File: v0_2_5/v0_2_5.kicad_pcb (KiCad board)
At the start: 2 copper layers, 91.4 x 50.8 mm, 58 parts, among them IC1 RASPBERRY_PI_PICO_W, IC2 BH1750FVI-TR, IC3 AP2138N-3.3TRG1, J1 S2B-PH-SM4-TB_LF__SN_, J2 HYCW110-TF10-180B, J4 SM04B-SRSS-TB, J5 Screw_Terminal_01x03, J6 Conn_01x02_Pin, Q1 DMG2301L-7, Q2 DMG2301L-7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

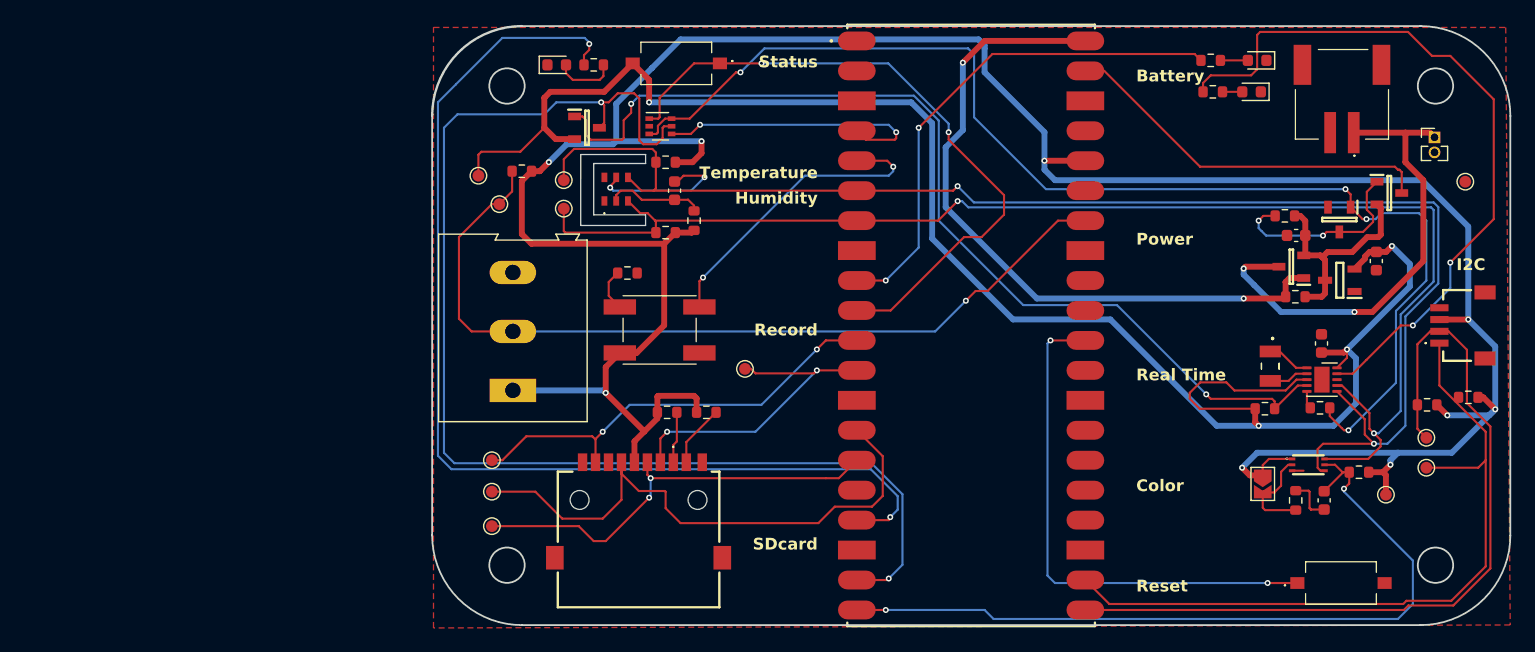
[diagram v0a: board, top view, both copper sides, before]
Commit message: replace sdcard
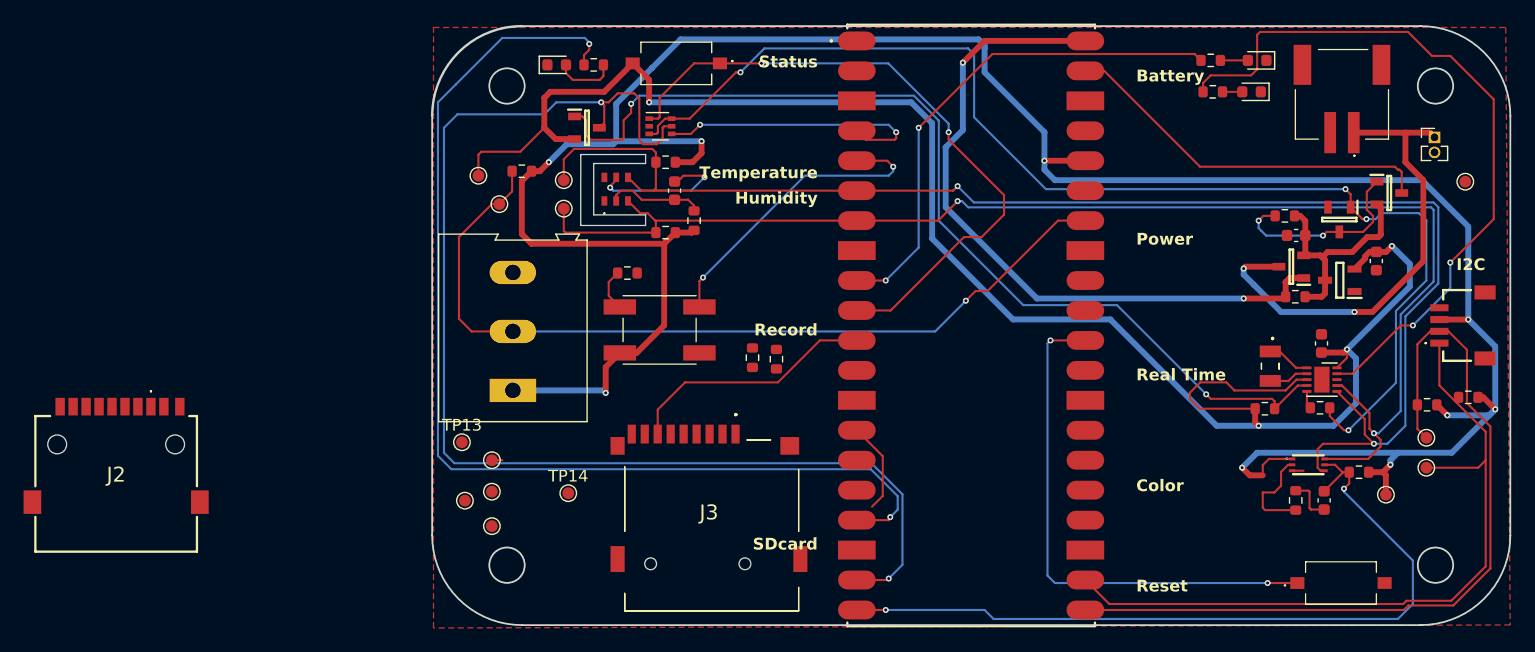
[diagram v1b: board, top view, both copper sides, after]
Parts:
- removed JP1: SolderJumper_2_Open, Jumper:SolderJumper-2_P1.3mm_Open_TrianglePad1.0x1.5mm
- added J3: TF-115, TF-115:TF115, F.Cu at (124.0, 113.1)
- added TP13: TestPoint, TestPoint:TestPoint_Pad_D1.0mm, F.Cu at (103.0, 107.2)
- added TP14: TestPoint, TestPoint:TestPoint_Pad_D1.0mm, F.Cu at (112.0, 111.5)
- moved J2 44.6 mm to (73.7, 110.7)
- moved TP6 26.2 mm to (103.3, 112.1)
- moved R10 8.60 mm to (127.6, 100.0), turned to -90 degrees
- moved R9 7.46 mm to (129.7, 100.1), turned to -90 degrees
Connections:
- J2 pad 1: /SDcard/DAT2 -> /SDcard/CARDDET
- R10 pad 2: /SDcard/DAT2 -> /SDcard/CARDDET
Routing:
- net /SCK: track 48.9 -> 7.76 mm
- net /MOSI: track 36.7 -> 0.00 mm, vias 2 -> 0
- net /CS: track 27.4 -> 0.00 mm, vias 2 -> 0
- net +3.3V: track 231.0 -> 215.4 mm
- net /MISO: track 37.3 -> 22.3 mm, vias 2 -> 0
- net /SDcard/CARDDET: track 5.28 -> 0.00 mm
- net /SDcard/DAT2: track 4.36 -> 0.00 mm

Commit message: replace sdcard
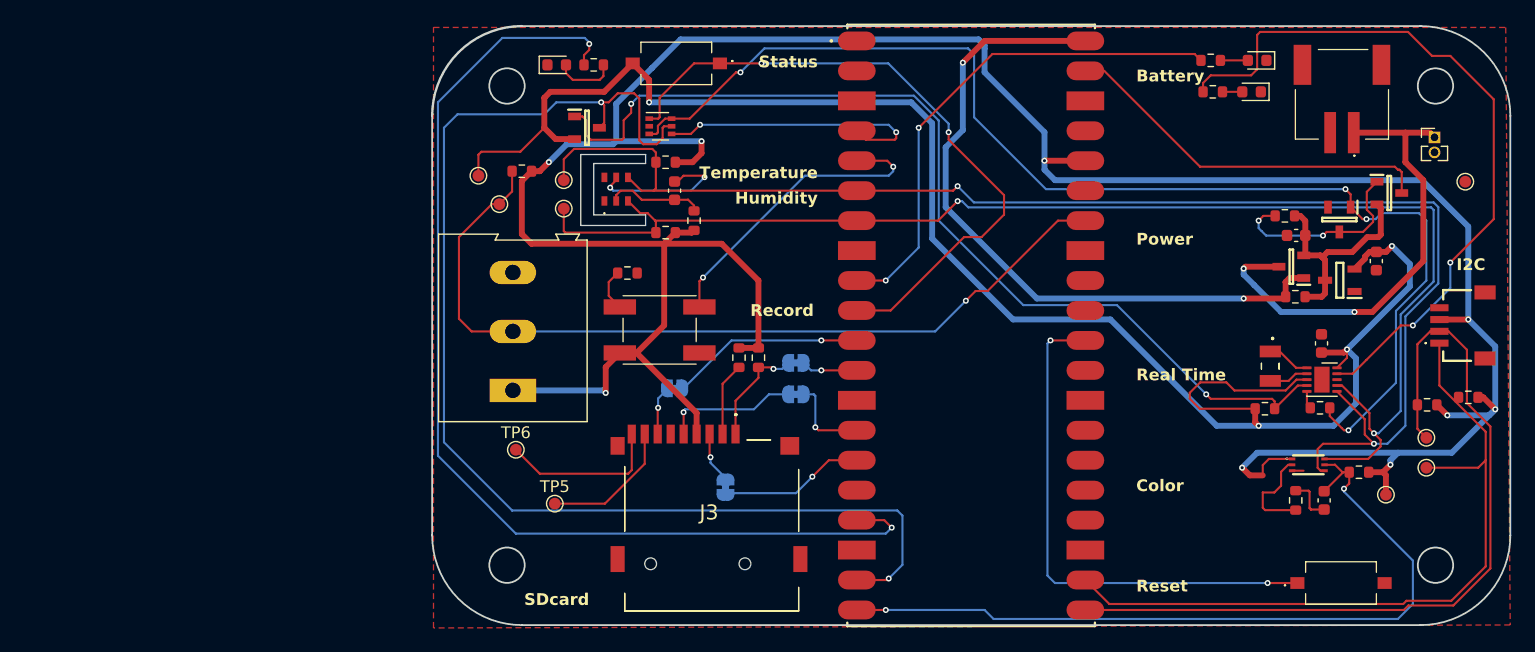
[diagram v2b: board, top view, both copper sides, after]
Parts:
- removed J2: HYCW110-TF10-180B, HYCW110-TF10-180B:HYCW110TF10180B
- removed TP13, TP14, TP7, TP8: TestPoint, TestPoint:TestPoint_Pad_D1.0mm
- added JP2: Jumper_2_Bridged, Jumper:SolderJumper-2_P1.3mm_Bridged_RoundedPad1.0x1.5mm, B.Cu at (131.3, 103.1)
- added JP3: Jumper_2_Bridged, Jumper:SolderJumper-2_P1.3mm_Bridged_RoundedPad1.0x1.5mm, B.Cu at (121.0, 102.6)
- added JP4: Jumper_2_Bridged, Jumper:SolderJumper-2_P1.3mm_Bridged_RoundedPad1.0x1.5mm, B.Cu at (131.3, 100.4)
- added JP8: Jumper_2_Bridged, Jumper:SolderJumper-2_P1.3mm_Bridged_RoundedPad1.0x1.5mm, B.Cu at (125.4, 111.0)
- moved TP6 6.11 mm to (107.6, 107.8)
- moved TP5 5.66 mm to (110.9, 112.4)
- moved R9 1.53 mm to (128.1, 100.0)
- moved R10 1.14 mm to (126.5, 100.0)
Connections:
- J3 pad 2: /CS -> Net-(J3-CD/DAT3)
- J3 pad 3: /SCK -> /MOSI
- J3 pad 7: /MISO -> Net-(J3-DAT0)
- J3 pad 8: /SDcard/DAT1 -> Net-(J3-DAT1)
- R10 pad 2: /SDcard/CARDDET -> Net-(J3-CD/DAT3)
- TP5 pad 1: /MOSI -> Net-(J3-DAT1)
- TP6 pad 1: /CS -> Net-(J3-PadCD1)
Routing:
- net +3.3V: track 215.4 -> 241.0 mm
- net /MOSI: track 0.00 -> 17.9 mm, vias 0 -> 2
- net Net-(J3-PadCD1): track 0.00 -> 13.9 mm
- net /SCK: track 7.76 -> 20.4 mm, vias 0 -> 2
- net Net-(J3-DAT1): track 0.00 -> 11.5 mm
- net /SDcard/CARDDET: track 0.00 -> 9.25 mm, vias 0 -> 1
- net Net-(J3-CD/DAT3): track 0.00 -> 6.23 mm
- net /MISO: track 22.3 -> 16.6 mm, vias 0 -> 1
- net /CS: track 0.00 -> 4.78 mm, vias 0 -> 1
- net Net-(J3-DAT0): track 0.00 -> 4.20 mm, vias 0 -> 1
- net /RTC_ALARM: track 106.3 -> 104.7 mm
- net /Record: track 92.9 -> 92.1 mm
